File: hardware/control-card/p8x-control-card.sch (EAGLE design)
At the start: 58 parts, among them J1 FABC96R, U1 CLK DIV, U10 UCODE ROM0, U11 UCODE ROM1, U12 UCODE ROM2, U13 UCODE ROM3, U14 PIPE0, U15 PIPE1, U16 PIPE2, U17 PIPE3, U18 STEP CNT, U19 74HCT86 NV-XOR, U2 74HCT14, U20 IRQ-FORCE DNP, U21 IRQ/IE FF DNP, U3 74HCT74, U4 74HCT00, U5 74HCT08, U6 74HCT32, U7 IR 74HCT377, U8 DLD DEC, U9 COND MUX, X1 4MHZ

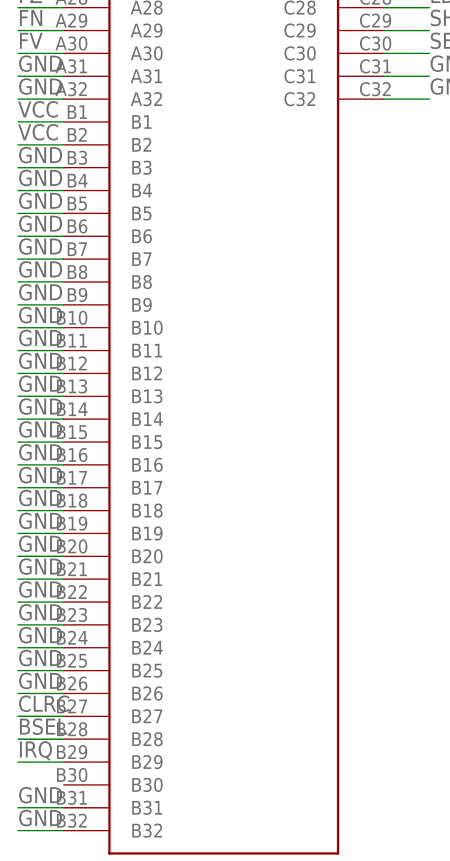
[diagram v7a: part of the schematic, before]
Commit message: feat(backplane): row-B even pins become spare bus lines (SPARE12-23)
Row B was a solid ground guard (B3-26 all GND). Per request, B3-26 now ALTERNATE:
odd pins stay GND (still a guard between most signal pairs), and the 12 even pins
(B4,B6,..,B26) become spare bus lines SPARE12-SPARE23, routed slot-to-slot — so
new signals can be added later without re-spinning the backplane. B27-30
(CLRC/BSEL/IRQ/SPARE11) unchanged.

- busnet() updated in all three copies (gen_eagle, gen_bus_pdf, gen_bus_card)
- backplane .brd routes the 12 new spares (mirrors the B27-30 routing); odd-pin
  grounds remain on the GND pour
- every card regenerated: their connectors no longer tie the even B pins to GND
  (those are spare lines now) — they simply don't connect the spares
- all 8 boards validate (0 errors); schematic + bus PDFs regenerated
- docs updated: bus-definition (pin map + notes), backplane theory + design notes
- net signal-integrity trade noted: a solid guard shields slightly better; the
  alternation was chosen deliberately for expansion room

Co-Authored-By: Claude Opus 4.8 <noreply@anthropic.com>
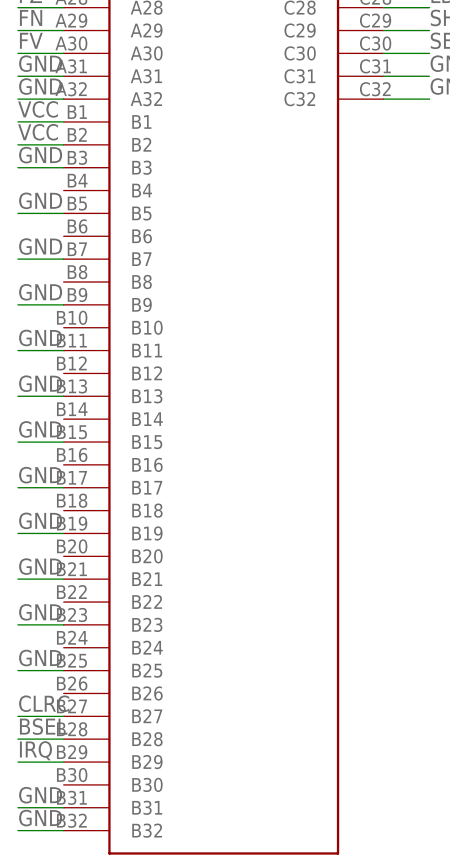
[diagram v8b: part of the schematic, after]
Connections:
- net GND: no longer J1.B10, J1.B12, J1.B14, J1.B16, J1.B18, J1.B20, J1.B22, J1.B24, J1.B26, J1.B4, J1.B6, J1.B8
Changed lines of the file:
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@@
 <wire x1="-17.78" y1="-48.26" x2="-22.86" y2="-48.26" width="0.1524" layer="91"/>
 <label x="-22.86" y="-47.75" size="1.778" layer="95"/></segment>
-<segment><pinref part="J1" gate="G$1" pin="B4"/>
-<wire x1="-17.78" y1="-50.80" x2="-22.86" y2="-50.80" width="0.1524" layer="91"/>
-<label x="-22.86" y="-50.29" size="1.778" layer="95"/></segment>
 <segment><pinref part="J1" gate="G$1" pin="B5"/>
 <wire x1="-17.78" y1="-53.34" x2="-22.86" y2="-53.34" width="0.1524" layer="91"/>
 <label x="-22.86" y="-52.83" size="1.778" layer="95"/></segment>
-<segment><pinref part="J1" gate="G$1" pin="B6"/>
-<wire x1="-17.78" y1="-55.88" x2="-22.86" y2="-55.88" width="0.1524" layer="91"/>
-<label x="-22.86" y="-55.37" size="1.778" layer="95"/></segment>
 <segment><pinref part="J1" gate="G$1" pin="B7"/>
 <wire x1="-17.78" y1="-58.42" x2="-22.86" y2="-58.42" width="0.1524" layer="91"/>
 <label x="-22.86" y="-57.91" size="1.778" layer="95"/></segment>
-<segment><pinref part="J1" gate="G$1" pin="B8"/>
-<wire x1="-17.78" y1="-60.96" x2="-22.86" y2="-60.96" width="0.1524" layer="91"/>
-<label x="-22.86" y="-60.45" size="1.778" layer="95"/></segment>
 <segment><pinref part="J1" gate="G$1" pin="B9"/>
 <wire x1="-17.78" y1="-63.50" x2="-22.86" y2="-63.50" width="0.1524" layer="91"/>
 <label x="-22.86" y="-62.99" size="1.778" layer="95"/></segment>
-<segment><pinref part="J1" gate="G$1" pin="B10"/>
-<wire x1="-17.78" y1="-66.04" x2="-22.86" y2="-66.04" width="0.1524" layer="91"/>
-<label x="-22.86" y="-65.53" size="1.778" layer="95"/></segment>
 <segment><pinref part="J1" gate="G$1" pin="B11"/>
 <wire x1="-17.78" y1="-68.58" x2="-22.86" y2="-68.58" width="0.1524" layer="91"/>
 <label x="-22.86" y="-68.07" size="1.778" layer="95"/></segment>
-<segment><pinref part="J1" gate="G$1" pin="B12"/>
-<wire x1="-17.78" y1="-71.12" x2="-22.86" y2="-71.12" width="0.1524" layer="91"/>
-<label x="-22.86" y="-70.61" size="1.778" layer="95"/></segment>
 <segment><pinref part="J1" gate="G$1" pin="B13"/>
 <wire x1="-17.78" y1="-73.66" x2="-22.86" y2="-73.66" width="0.1524" layer="91"/>
 <label x="-22.86" y="-73.15" size="1.778" layer="95"/></segment>
-<segment><pinref part="J1" gate="G$1" pin="B14"/>
-<wire x1="-17.78" y1="-76.20" x2="-22.86" y2="-76.20" width="0.1524" layer="91"/>
-<label x="-22.86" y="-75.69" size="1.778" layer="95"/></segment>
 <segment><pinref part="J1" gate="G$1" pin="B15"/>
 <wire x1="-17.78" y1="-78.74" x2="-22.86" y2="-78.74" width="0.1524" layer="91"/>
 <label x="-22.86" y="-78.23" size="1.778" layer="95"/></segment>
-<segment><pinref part="J1" gate="G$1" pin="B16"/>
-<wire x1="-17.78" y1="-81.28" x2="-22.86" y2="-81.28" width="0.1524" layer="91"/>
-<label x="-22.86" y="-80.77" size="1.778" layer="95"/></segment>
 <segment><pinref part="J1" gate="G$1" pin="B17"/>
 <wire x1="-17.78" y1="-83.82" x2="-22.86" y2="-83.82" width="0.1524" layer="91"/>
 <label x="-22.86" y="-83.31" size="1.778" layer="95"/></segment>
-<segment><pinref part="J1" gate="G$1" pin="B18"/>
-<wire x1="-17.78" y1="-86.36" x2="-22.86" y2="-86.36" width="0.1524" layer="91"/>
-<label x="-22.86" y="-85.85" size="1.778" layer="95"/></segment>
 <segment><pinref part="J1" gate="G$1" pin="B19"/>
 <wire x1="-17.78" y1="-88.90" x2="-22.86" y2="-88.90" width="0.1524" layer="91"/>
 <label x="-22.86" y="-88.39" size="1.778" layer="95"/></segment>
-<segment><pinref part="J1" gate="G$1" pin="B20"/>
-<wire x1="-17.78" y1="-91.44" x2="-22.86" y2="-91.44" width="0.1524" layer="91"/>
-<label x="-22.86" y="-90.93" size="1.778" layer="95"/></segment>
 <segment><pinref part="J1" gate="G$1" pin="B21"/>
 <wire x1="-17.78" y1="-93.98" x2="-22.86" y2="-93.98" width="0.1524" layer="91"/>
 <label x="-22.86" y="-93.47" size="1.778" layer="95"/></segment>
-<segment><pinref part="J1" gate="G$1" pin="B22"/>
-<wire x1="-17.78" y1="-96.52" x2="-22.86" y2="-96.52" width="0.1524" layer="91"/>
-<label x="-22.86" y="-96.01" size="1.778" layer="95"/></segment>
 <segment><pinref part="J1" gate="G$1" pin="B23"/>
 <wire x1="-17.78" y1="-99.06" x2="-22.86" y2="-99.06" width="0.1524" layer="91"/>
 <label x="-22.86" y="-98.55" size="1.778" layer="95"/></segment>
-<segment><pinref part="J1" gate="G$1" pin="B24"/>
-<wire x1="-17.78" y1="-101.60" x2="-22.86" y2="-101.60" width="0.1524" layer="91"/>
-<label x="-22.86" y="-101.09" size="1.778" layer="95"/></segment>
 <segment><pinref part="J1" gate="G$1" pin="B25"/>
 <wire x1="-17.78" y1="-104.14" x2="-22.86" y2="-104.14" width="0.1524" layer="91"/>
 <label x="-22.86" y="-103.63" size="1.778" layer="95"/></segment>
-<segment><pinref part="J1" gate="G$1" pin="B26"/>
-<wire x1="-17.78" y1="-106.68" x2="-22.86" y2="-106.68" width="0.1524" layer="91"/>
-<label x="-22.86" y="-106.17" size="1.778" layer="95"/></segment>
 <segment><pinref part="J1" gate="G$1" pin="B31"/>
 <wire x1="-17.78" y1="-119.38" x2="-22.86" y2="-119.38" width="0.1524" layer="91"/>
